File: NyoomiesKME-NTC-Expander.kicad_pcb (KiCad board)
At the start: 2 copper layers, 30.5 x 14 mm, 9 parts, among them J1 2x4 Dupont Socket, J2 JST XH 2 Pin, J3 JST XH 2 Pin, J4 JST XH 2 Pin, J5 JST XH 2 Pin

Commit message: smaller routing fixes, relocate R3 R4
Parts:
- moved R3 1.28 mm to (146.8, 105.8)
- moved R4 1.09 mm to (152.2, 105.8)
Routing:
- net +3.3V: track 23.7 -> 19.7 mm
- net A4: track 12.0 -> 10.1 mm
- net A3: track 14.7 -> 13.5 mm
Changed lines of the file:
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@@
 	(footprint "Resistor_SMD:R_1206_3216Metric"
 		(layer "F.Cu")
-		(at 145.75 106.5)
+		(at 146.7875 105.75)
 		(descr "Resistor SMD 1206 (3216 Metric), square (rectangular) end terminal, IPC_7351 nominal, (Body size source: IPC-SM-782 page 72, https://www.pcb-3d.com/wordpress/wp-content/uploads/ipc-sm-782a_amendment_1_and_2.pdf), generated with kicad-footprint-generator")
 		(tags "resistor")
 		(property "Reference" "R3"
-			(at 1.5 -1.75 180)
+			(at -3.0375 1 -90)
 			(layer "F.SilkS")
 			(effects
@@
 		)
 		(property "Value" "R4.7k"
-			(at 0 2.75 0)
+			(at 0 4 0)
 			(layer "F.Fab")
 			(effects
@@
 	(footprint "Resistor_SMD:R_1206_3216Metric"
 		(layer "F.Cu")
-		(at 153 106.5 180)
+		(at 152.2125 105.75 180)
 		(descr "Resistor SMD 1206 (3216 Metric), square (rectangular) end terminal, IPC_7351 nominal, (Body size source: IPC-SM-782 page 72, https://www.pcb-3d.com/wordpress/wp-content/uploads/ipc-sm-782a_amendment_1_and_2.pdf), generated with kicad-footprint-generator")
 		(tags "resistor")
 		(property "Reference" "R4"
-			(at 1.5 1.75 180)
+			(at -3.2875 -1 90)
 			(layer "F.SilkS")
 			(effects
@@
 		)
 		(property "Value" "R4.7k"
-			(at 0 -2.75 0)
+			(at 0 -4 0)
 			(layer "F.Fab")
 			(effects
@@
 	)
 	(gr_text "PA3"
-		(at 144 105.5 90)
+		(at 144 104.25 90)
 		(layer "F.SilkS")
 		(effects
@@
 	)
 	(gr_text "PA1"
-		(at 144 98.75 90)
+		(at 144 100.5 90)
 		(layer "F.SilkS")
 		(effects
@@
 	)
 	(gr_text "PA2"
-		(at 155 96 -90)
+		(at 155 97.75 -90)
 		(layer "F.SilkS")
 		(effects
@@
 	)
 	(gr_text "PA4"
-		(at 155 102.5 -90)
+		(at 155 101.25 -90)
 		(layer "F.SilkS")
 		(effects
@@
 	)
 	(segment
-		(start 149.5 101.75)
-		(end 152.04 101.75)
+		(start 147.315125 101.765125)
+		(end 149.515125 101.765125)
 		(width 0.3)
 		(layer "F.Cu")
@@
 	)
 	(segment
-		(start 152.04 101.75)
-		(end 152.09 101.7)
+		(start 149.5 101.78025)
+		(end 149.5 104.5)
 		(width 0.3)
 		(layer "F.Cu")
@@
 	)
 	(segment
-		(start 146.5 98.2125)
-		(end 146.87 98.5825)
-		(width 0.3)
-		(layer "F.Cu")
-		(net 2)
-	)
-	(segment
-		(start 146.87 100.857057)
-		(end 147.762943 101.75)
-		(width 0.3)
-		(layer "F.Cu")
-		(net 2)
-	)
-	(segment
-		(start 147.9625 107.25)
-		(end 150.7875 107.25)
+		(start 146.936845 98.649345)
+		(end 146.936845 101.386845)
 		(width 0.3)
 		(layer "F.Cu")
@@
 	)
 	(segment
-		(start 150.7875 107.25)
-		(end 151.5375 106.5)
+		(start 153.29 100.5)
+		(end 152.024875 101.765125)
 		(width 0.3)
 		(layer "F.Cu")
@@
 	)
 	(segment
-		(start 147.762943 101.75)
-		(end 149.5 101.75)
+		(start 152.024875 101.765125)
+		(end 149.515125 101.765125)
 		(width 0.3)
 		(layer "F.Cu")
@@
 	)
 	(segment
-		(start 147.2125 106.5)
-		(end 147.9625 107.25)
+		(start 146.936845 101.386845)
+		(end 147.315125 101.765125)
 		(width 0.3)
 		(layer "F.Cu")
@@
 	)
 	(segment
-		(start 149.5 104.4625)
-		(end 151.5375 106.5)
+		(start 146.5 98.2125)
+		(end 146.936845 98.649345)
 		(width 0.3)
 		(layer "F.Cu")
@@
 	)
 	(segment
-		(start 149.5 101.75)
-		(end 149.5 104.2125)
+		(start 149.5 104.5)
+		(end 150.75 105.75)
 		(width 0.3)
 		(layer "F.Cu")
@@
 	)
 	(segment
-		(start 152.09 101.7)
-		(end 153.29 100.5)
+		(start 149.515125 101.765125)
+		(end 149.5 101.78025)
 		(width 0.3)
 		(layer "F.Cu")
@@
 	)
 	(segment
-		(start 146.87 98.5825)
-		(end 146.87 100.857057)
-		(width 0.3)
-		(layer "F.Cu")
-		(net 2)
-	)
-	(segment
-		(start 149.5 104.2125)
-		(end 149.5 104.4625)
+		(start 149.5 104.5)
+		(end 148.25 105.75)
 		(width 0.3)
 		(layer "F.Cu")
@@
 	)
 	(segment
-		(start 139.75 96.975)
-		(end 142.275 96.975)
+		(start 145.67 100.42)
+		(end 145.67 100.5)
 		(width 0.3)
 		(layer "F.Cu")
@@
 	(segment
 		(start 139.75 96.975)
-		(end 142.225 96.975)
+		(end 142.275 96.975)
 		(width 0.3)
-		(layer "B.Cu")
+		(layer "F.Cu")
 		(net 3)
 	)
 	(segment
-		(start 145.67 100.42)
-		(end 145.67 100.5)
+		(start 139.75 96.975)
+		(end 142.225 96.975)
 		(width 0.3)
 		(layer "B.Cu")
@@
 	)
 	(segment
-		(start 137.25 105.5)
-		(end 138.25 106.5)
-		(width 0.3)
-		(layer "F.Cu")
-		(net 4)
-	)
-	(segment
-		(start 148.21 105.04)
-		(end 148 105.25)
-		(width 0.3)
-		(layer "F.Cu")
-		(net 4)
-	)
-	(segment
-		(start 146.669544 105.25)
-		(end 145.419544 106.5)
+		(start 145.5 105.75)
+		(end 145.325 105.75)
 		(width 0.3)
 		(layer "F.Cu")
@@
 	)
 	(segment
-		(start 145.419544 106.5)
-		(end 144.2875 106.5)
+		(start 144.325 106.75)
+		(end 138.975 106.75)
 		(width 0.3)
 		(layer "F.Cu")
@@
 	)
 	(segment
-		(start 137.25 105.025)
-		(end 137.25 105.5)
+		(start 138.975 106.75)
+		(end 137.25 105.025)
 		(width 0.3)
 		(layer "F.Cu")
@@
 	)
 	(segment
-		(start 148 105.25)
-		(end 146.669544 105.25)
+		(start 148.21 103.04)
+		(end 145.5 105.75)
 		(width 0.3)
 		(layer "F.Cu")
@@
 	)
 	(segment
-		(start 148.21 103.04)
-		(end 148.21 105.04)
-		(width 0.3)
-		(layer "F.Cu")
-		(net 4)
-	)
-	(segment
-		(start 138.25 106.5)
-		(end 144.2875 106.5)
+		(start 145.325 105.75)
+		(end 144.325 106.75)
 		(width 0.3)
 		(layer "F.Cu")
@@
 	)
 	(segment
-		(start 150.75 104.5)
-		(end 151.25 105)
-		(width 0.3)
-		(layer "F.Cu")
-		(net 8)
-	)
-	(segment
-		(start 152.5 105.669544)
-		(end 152.5 106)
+		(start 150.75 103.04)
+		(end 150.96 103.04)
 		(width 0.3)
 		(layer "F.Cu")
@@
 	)
 	(segment
-		(start 150.75 103.04)
-		(end 150.75 104.5)
-		(width 0.3)
-		(layer "F.Cu")
-		(net 8)
-	)
-	(segment
-		(start 157.75 106.5)
+		(start 159 105.25)
 		(end 159.25 105)
 		(width 0.3)
@@
 	)
 	(segment
-		(start 151.25 105)
-		(end 151.830456 105)
-		(width 0.3)
-		(layer "F.Cu")
-		(net 8)
-	)
-	(segment
-		(start 154.4625 106.5)
-		(end 157.75 106.5)
+		(start 150.96 103.04)
+		(end 151 103)
 		(width 0.3)
 		(layer "F.Cu")
@@
 	)
 	(segment
-		(start 151.830456 105)
-		(end 152.5 105.669544)
+		(start 151 103)
+		(end 151 103.075)
 		(width 0.3)
 		(layer "F.Cu")
@@
 	)
 	(segment
-		(start 152.5 106)
-		(end 153 106.5)
+		(start 154.175 105.25)
+		(end 159 105.25)
 		(width 0.3)
 		(layer "F.Cu")
@@
 	)
 	(segment
-		(start 154.4625 106.5)
-		(end 154.7125 106.75)
+		(start 153.675 105.75)
+		(end 154.175 105.25)
 		(width 0.3)
 		(layer "F.Cu")
@@
 	)
 	(segment
-		(start 153 106.5)
-		(end 154.4625 106.5)
+		(start 151 103.075)
+		(end 153.675 105.75)
 		(width 0.3)
 		(layer "F.Cu")

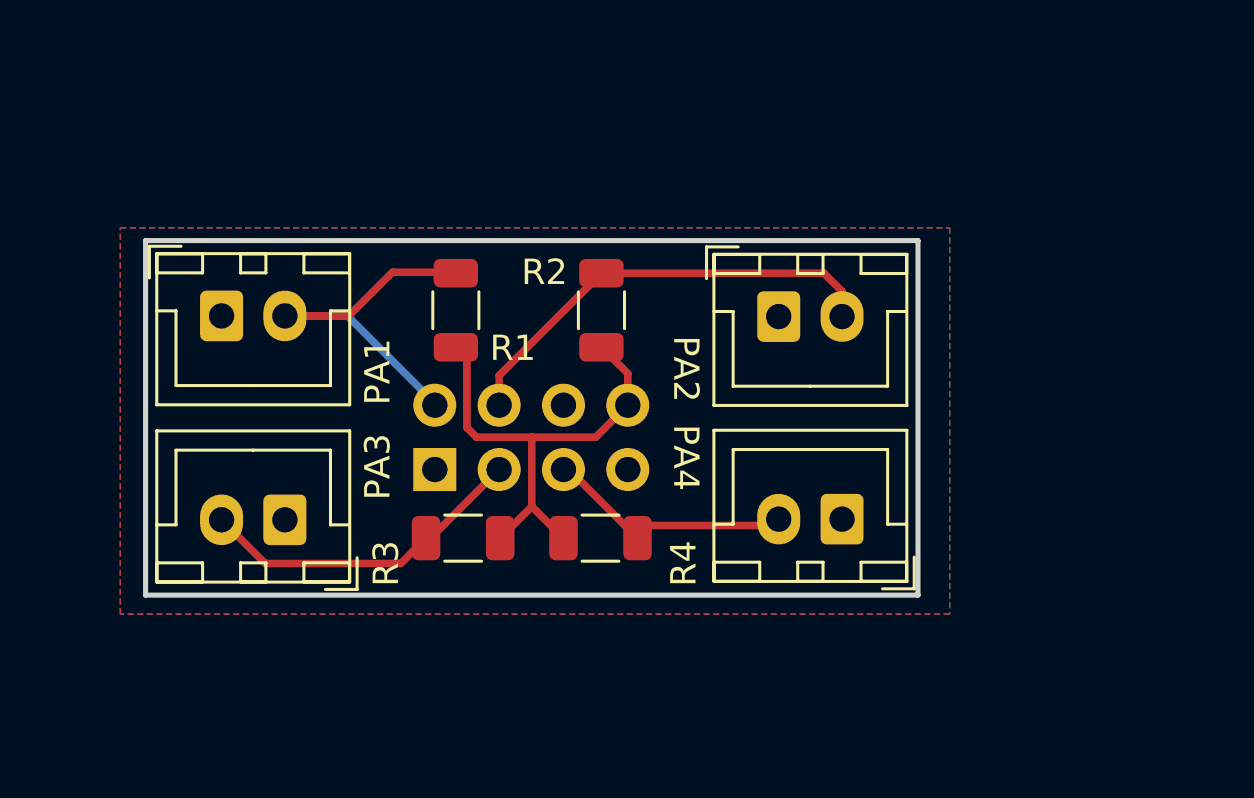
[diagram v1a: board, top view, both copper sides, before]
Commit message: rev 0.2: add filter caps
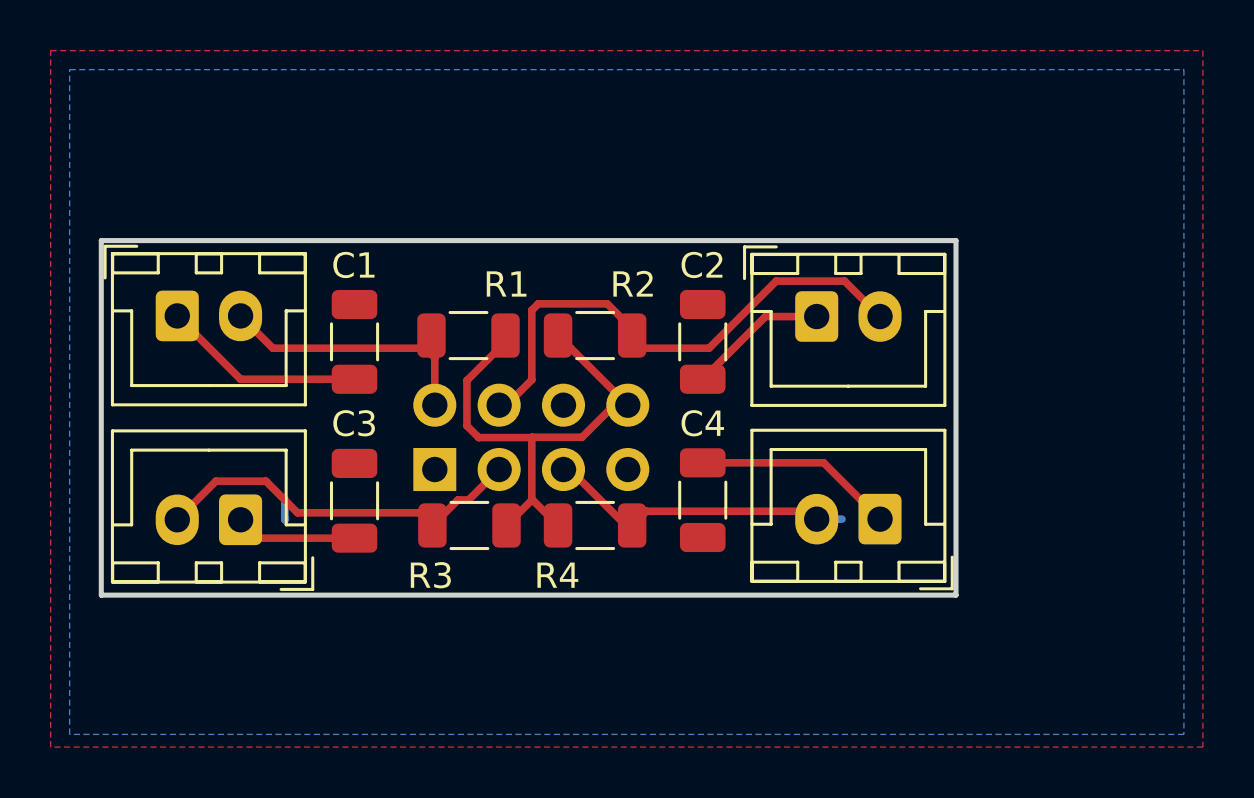
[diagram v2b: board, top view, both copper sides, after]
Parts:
- added C1: 10u, Capacitor_SMD:C_1206_3216Metric, F.Cu at (142.5, 98.0)
- added C2: 10u, Capacitor_SMD:C_1206_3216Metric, F.Cu at (156.2, 98.0)
- added C3: 10u, Capacitor_SMD:C_1206_3216Metric, F.Cu at (142.5, 104.3)
- added C4: 10u, Capacitor_SMD:C_1206_3216Metric, F.Cu at (156.2, 104.2)
- R1, R2, R3, R4: value R4.7k -> 4.7k
- moved J2 1.75 mm to (135.5, 97.0)
- moved J4 1.75 mm to (138.0, 105.0)
- moved J3 1.50 mm to (160.8, 97.0)
- moved J5 1.50 mm to (163.2, 105.0)
- moved R1 1.12 mm to (147.0, 97.8), turned to 0 degrees
- moved R2 1.03 mm to (152.0, 97.8), turned to 180 degrees
- moved R3 0.56 mm to (147.0, 105.2)
- moved R4 0.54 mm to (152.0, 105.2)
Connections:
- J2 pad 1: GND -> Net-(J2-Pin_1)
- J3 pad 1: GND -> Net-(J3-Pin_1)
- J4 pad 1: GND -> Net-(J4-Pin_1)
- J5 pad 1: GND -> Net-(J5-Pin_1)
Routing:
- net Net-(J2-Pin_1): track 0.00 -> 8.04 mm
- net Net-(J5-Pin_1): track 0.00 -> 7.92 mm
- net Net-(J3-Pin_1): track 0.00 -> 5.53 mm
- net Net-(J4-Pin_1): track 0.00 -> 4.84 mm
- net A1: track 14.2 -> 10.3 mm
- net A2: track 18.7 -> 21.7 mm
- net A3: track 13.5 -> 15.8 mm
- net A4: track 10.1 -> 12.0 mm
- net GND: track 1.61 -> 0.86 mm
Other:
- board size 30.5 x 14 mm -> 33.8 x 14 mm
- board text added: "HW Rev 0.2"
- board text removed: "HW Rev 0.1"

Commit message: switch to 2.2k, fix pcb DRC
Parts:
- R1, R2, R3, R4: value 4.7k -> 2.2k
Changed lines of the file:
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@@
 			)
 		)
-		(property "Value" "4.7k"
+		(property "Value" "2.2k"
 			(at -0.0375 4 0)
 			(layer "F.Fab")
@@
 			)
 		)
-		(property "LCSC Part #" "C17936"
+		(property "LCSC Part #" "C311944"
 			(at 0 0 0)
 			(unlocked yes)
@@
 			)
 		)
-		(property "Value" "4.7k"
+		(property "Value" "2.2k"
 			(at 0 -4 0)
 			(layer "F.Fab")
@@
 			)
 		)
-		(property "LCSC Part #" "C17936"
+		(property "LCSC Part #" "C311944"
 			(at 0 0 180)
 			(unlocked yes)
@@
 			)
 		)
-		(property "Value" "4.7k"
+		(property "Value" "2.2k"
 			(at 0 -5 180)
 			(layer "F.Fab")
@@
 			)
 		)
-		(property "LCSC Part #" "C17936"
+		(property "LCSC Part #" "C311944"
 			(at 0 0 0)
 			(unlocked yes)
@@
 			)
 		)
-		(property "Value" "4.7k"
+		(property "Value" "2.2k"
 			(at 0 5 180)
 			(layer "F.Fab")
@@
 			)
 		)
-		(property "LCSC Part #" "C17936"
+		(property "LCSC Part #" "C311944"
 			(at 0 0 180)
 			(unlocked yes)
@@
 	)
 	(gr_text "PA3"
-		(at 138.5 104 0)
+		(at 136.75 103.75 0)
 		(layer "B.SilkS")
 		(effects
@@
 	)
 	(gr_text "PA1"
-		(at 138.5 99.25 0)
+		(at 136.75 99.5 0)
 		(layer "B.SilkS")
 		(effects
@@
 	)
 	(gr_text "PA2"
-		(at 160.5 99.25 0)
+		(at 162 99.5 0)
 		(layer "B.SilkS")
 		(effects
@@
 	)
 	(gr_text "PA4"
-		(at 160.5 104 0)
+		(at 161.75 103.75 0)
 		(layer "B.SilkS")
 		(effects
@@
 		(net 8)
 	)
-	(segment
-		(start 161.5 105)
-		(end 161.75 105)
-		(width 0.3)
-		(layer "B.Cu")
-		(net 8)
-	)
